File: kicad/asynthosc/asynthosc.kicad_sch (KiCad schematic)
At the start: 34 parts

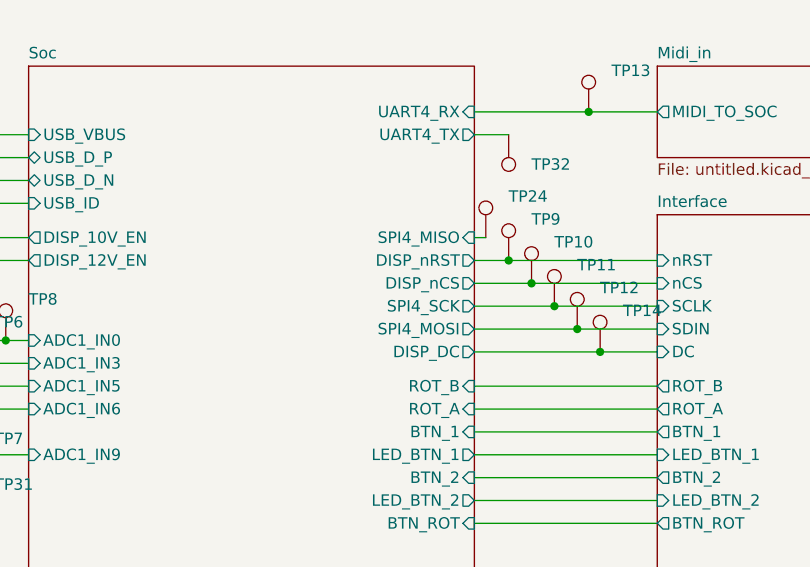
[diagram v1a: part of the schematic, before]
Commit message: fix: qspi ncs port issue, port naming
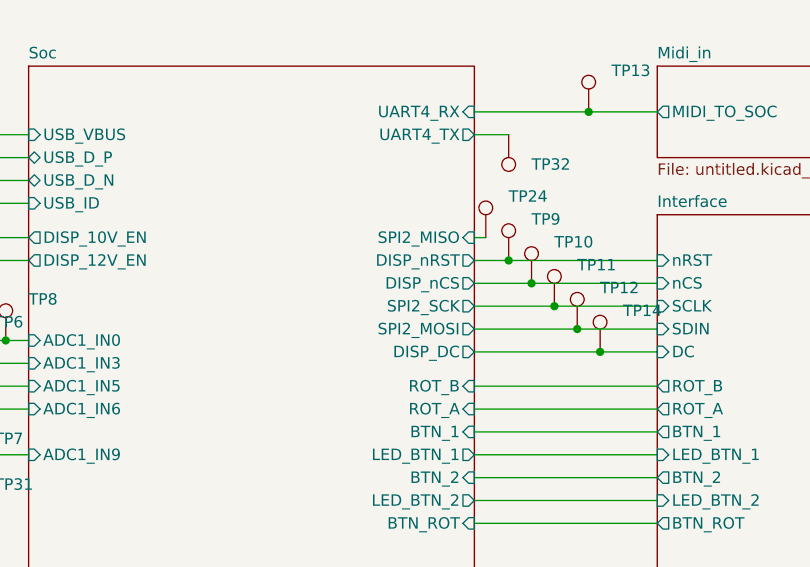
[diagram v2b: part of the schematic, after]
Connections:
- net Soc/SPI4_MISO renamed Soc/SPI2_MISO
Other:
- sheet Soc ports: added SPI2_MISO, SPI2_MOSI, SPI2_SCK; removed SPI4_MISO, SPI4_MOSI, SPI4_SCK
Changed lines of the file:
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@@
 			)
 		)
-		(pin "SPI4_MOSI" output
+		(pin "SPI2_MOSI" output
 			(at 176.53 100.33 0)
 			(effects
@@
 			)
 		)
-		(pin "SPI4_SCK" output
+		(pin "SPI2_SCK" output
 			(at 176.53 97.79 0)
 			(effects
@@
 			)
 		)
-		(pin "SPI4_MISO" input
+		(pin "SPI2_MISO" input
 			(at 176.53 90.17 0)
 			(effects
